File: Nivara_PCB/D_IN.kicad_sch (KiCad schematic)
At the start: 9 parts, among them U15 LTV-357T, U16 LTV-357T, U17 LTV-357T

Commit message: New changes to the Nivara PCB schematic files.
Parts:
- added D31, D32, D33: LED ON, LED_SMD:LED_0603_1608Metric, symbol Device:LED
- R43, R45, R47: value 10k -> 140
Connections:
- net ESP_D_IN_1: now also D31.1 (K); no longer R43.2
- net ESP_D_IN_2: now also D32.1 (K); no longer R45.2
- net ESP_RUN_IN: now also D33.1 (K); no longer R47.2
- new net: D31.2 (A), R43.2
- new net: D33.2 (A), R47.2
- new net: D32.2 (A), R45.2
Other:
- moved on the sheet: R42, R44, R46

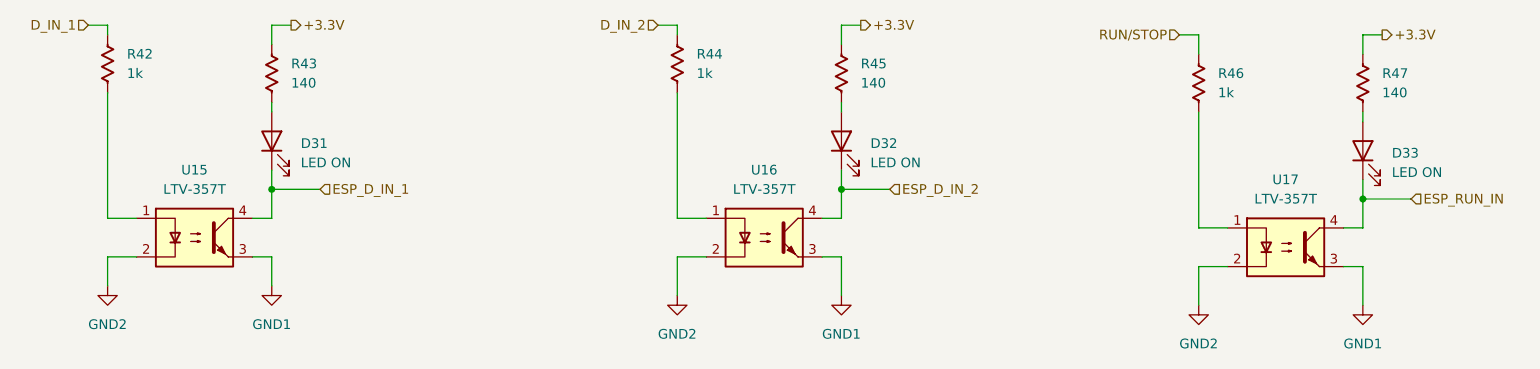
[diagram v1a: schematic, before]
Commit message: Cambios en el PCB de Nivara. Ruteo de emtradas y salidas NPN y PNP.
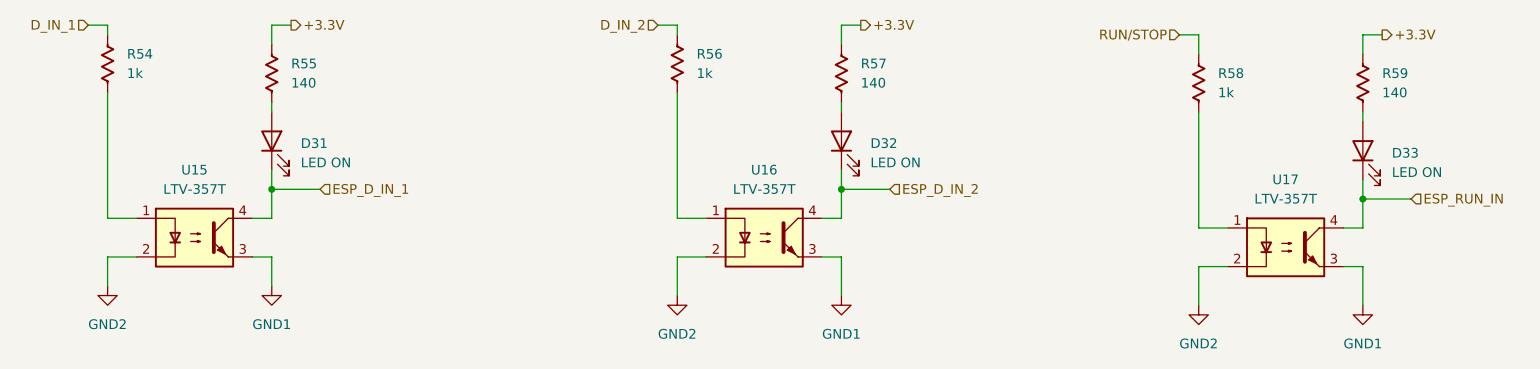
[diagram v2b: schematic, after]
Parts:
- renumbered R42 to R54, R43 to R55, R44 to R56, R45 to R57, R46 to R58, R47 to R59
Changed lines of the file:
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@@
 		(dnp no)
 		(fields_autoplaced yes)
-		(property "Reference" "R43"
+		(property "Reference" "R55"
 			(at 78.74 52.0699 0)
 			(effects
@@
 			(project "Nivara_PCB"
 				(path "/13184db0-a71d-4054-b13a-bbf46d2b100d/4e7fa7f2-8bf5-4f9c-874d-fa1b4fd76f92/a8a95db9-2db6-4dd5-a448-91db082870e6"
-					(reference "R43")
+					(reference "R55")
 					(unit 1)
 				)
@@
 		(dnp no)
 		(fields_autoplaced yes)
-		(property "Reference" "R46"
+		(property "Reference" "R58"
 			(at 200.66 53.3399 0)
 			(effects
@@
 			(project "Nivara_PCB"
 				(path "/13184db0-a71d-4054-b13a-bbf46d2b100d/4e7fa7f2-8bf5-4f9c-874d-fa1b4fd76f92/a8a95db9-2db6-4dd5-a448-91db082870e6"
-					(reference "R46")
+					(reference "R58")
 					(unit 1)
 				)
@@
 		(dnp no)
 		(fields_autoplaced yes)
-		(property "Reference" "R47"
+		(property "Reference" "R59"
 			(at 222.25 53.3399 0)
 			(effects
@@
 			(project "Nivara_PCB"
 				(path "/13184db0-a71d-4054-b13a-bbf46d2b100d/4e7fa7f2-8bf5-4f9c-874d-fa1b4fd76f92/a8a95db9-2db6-4dd5-a448-91db082870e6"
-					(reference "R47")
+					(reference "R59")
 					(unit 1)
 				)
@@
 		(dnp no)
 		(fields_autoplaced yes)
-		(property "Reference" "R44"
+		(property "Reference" "R56"
 			(at 132.08 50.7999 0)
 			(effects
@@
 			(project "Nivara_PCB"
 				(path "/13184db0-a71d-4054-b13a-bbf46d2b100d/4e7fa7f2-8bf5-4f9c-874d-fa1b4fd76f92/a8a95db9-2db6-4dd5-a448-91db082870e6"
-					(reference "R44")
+					(reference "R56")
 					(unit 1)
 				)
@@
 		(dnp no)
 		(fields_autoplaced yes)
-		(property "Reference" "R45"
+		(property "Reference" "R57"
 			(at 153.67 52.0699 0)
 			(effects
@@
 			(project "Nivara_PCB"
 				(path "/13184db0-a71d-4054-b13a-bbf46d2b100d/4e7fa7f2-8bf5-4f9c-874d-fa1b4fd76f92/a8a95db9-2db6-4dd5-a448-91db082870e6"
-					(reference "R45")
+					(reference "R57")
 					(unit 1)
 				)
@@
 		(dnp no)
 		(fields_autoplaced yes)
-		(property "Reference" "#PWR052"
+		(property "Reference" "#PWR073"
 			(at 129.54 88.9 0)
 			(effects
@@
 			(project "Nivara_PCB"
 				(path "/13184db0-a71d-4054-b13a-bbf46d2b100d/4e7fa7f2-8bf5-4f9c-874d-fa1b4fd76f92/a8a95db9-2db6-4dd5-a448-91db082870e6"
-					(reference "#PWR052")
+					(reference "#PWR073")
 					(unit 1)
 				)
@@
 		(dnp no)
 		(fields_autoplaced yes)
-		(property "Reference" "#PWR050"
+		(property "Reference" "#PWR071"
 			(at 54.61 87.63 0)
 			(effects
@@
 			(project "Nivara_PCB"
 				(path "/13184db0-a71d-4054-b13a-bbf46d2b100d/4e7fa7f2-8bf5-4f9c-874d-fa1b4fd76f92/a8a95db9-2db6-4dd5-a448-91db082870e6"
-					(reference "#PWR050")
+					(reference "#PWR071")
 					(unit 1)
 				)
@@
 		(dnp no)
 		(fields_autoplaced yes)
-		(property "Reference" "#PWR054"
+		(property "Reference" "#PWR075"
 			(at 198.12 90.17 0)
 			(effects
@@
 			(project "Nivara_PCB"
 				(path "/13184db0-a71d-4054-b13a-bbf46d2b100d/4e7fa7f2-8bf5-4f9c-874d-fa1b4fd76f92/a8a95db9-2db6-4dd5-a448-91db082870e6"
-					(reference "#PWR054")
+					(reference "#PWR075")
 					(unit 1)
 				)
@@
 		(dnp no)
 		(fields_autoplaced yes)
-		(property "Reference" "#PWR051"
+		(property "Reference" "#PWR072"
 			(at 76.2 87.63 0)
 			(effects
@@
 			(project "Nivara_PCB"
 				(path "/13184db0-a71d-4054-b13a-bbf46d2b100d/4e7fa7f2-8bf5-4f9c-874d-fa1b4fd76f92/a8a95db9-2db6-4dd5-a448-91db082870e6"
-					(reference "#PWR051")
+					(reference "#PWR072")
 					(unit 1)
 				)
@@
 		(dnp no)
 		(fields_autoplaced yes)
-		(property "Reference" "#PWR055"
+		(property "Reference" "#PWR076"
 			(at 219.71 90.17 0)
 			(effects
@@
 			(project "Nivara_PCB"
 				(path "/13184db0-a71d-4054-b13a-bbf46d2b100d/4e7fa7f2-8bf5-4f9c-874d-fa1b4fd76f92/a8a95db9-2db6-4dd5-a448-91db082870e6"
-					(reference "#PWR055")
+					(reference "#PWR076")
 					(unit 1)
 				)
@@
 		(dnp no)
 		(fields_autoplaced yes)
-		(property "Reference" "#PWR053"
+		(property "Reference" "#PWR074"
 			(at 151.13 88.9 0)
 			(effects
@@
 			(project "Nivara_PCB"
 				(path "/13184db0-a71d-4054-b13a-bbf46d2b100d/4e7fa7f2-8bf5-4f9c-874d-fa1b4fd76f92/a8a95db9-2db6-4dd5-a448-91db082870e6"
-					(reference "#PWR053")
+					(reference "#PWR074")
 					(unit 1)
 				)
@@
 		(dnp no)
 		(fields_autoplaced yes)
-		(property "Reference" "R42"
+		(property "Reference" "R54"
 			(at 57.15 50.7999 0)
 			(effects
@@
 			(project "Nivara_PCB"
 				(path "/13184db0-a71d-4054-b13a-bbf46d2b100d/4e7fa7f2-8bf5-4f9c-874d-fa1b4fd76f92/a8a95db9-2db6-4dd5-a448-91db082870e6"
-					(reference "R42")
-					(unit 1)
-				)
+					(reference "R54")
+					(unit 1)
+				)
